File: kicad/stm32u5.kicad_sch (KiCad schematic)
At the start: 10 parts, among them SW5 BOOTSEL, U12 STM32U535CET6-modified

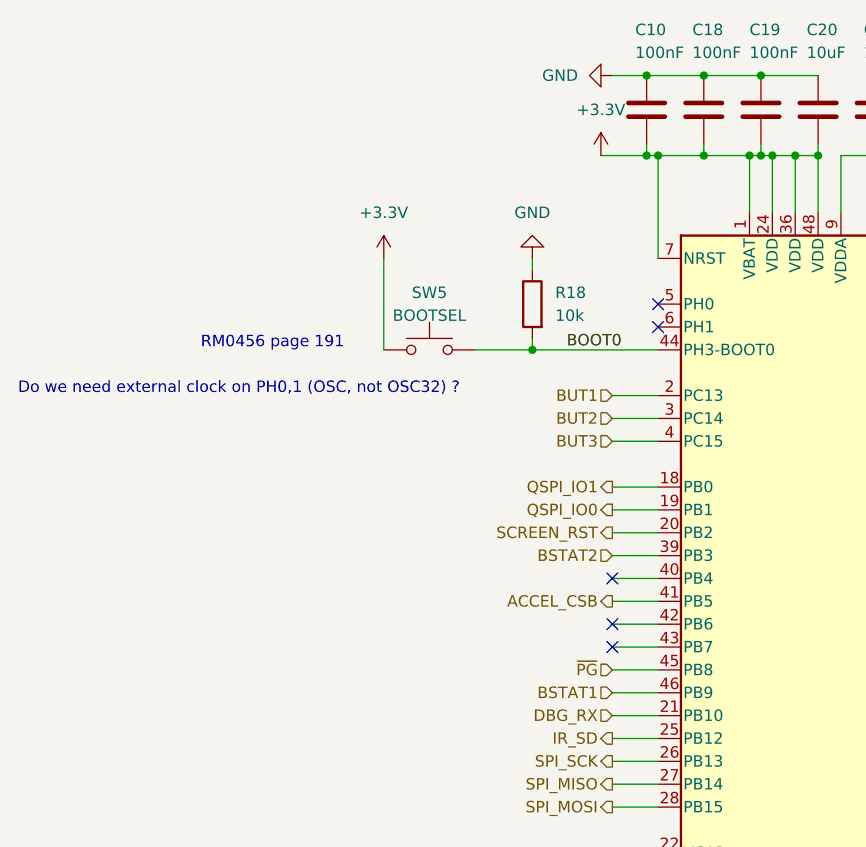
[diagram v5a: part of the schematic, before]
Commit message: hw: change battery to a "simpler" version
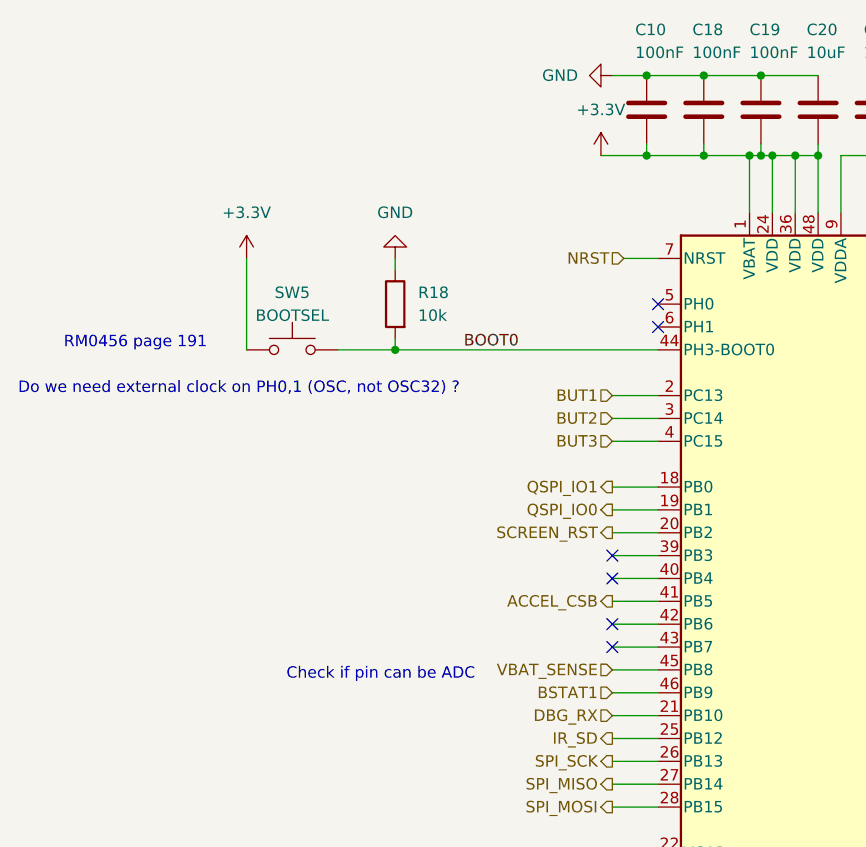
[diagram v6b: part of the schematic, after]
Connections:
- net +3.3V: no longer U12.7 (NRST)
- net BSTAT2: no longer names the net of U12.39 (PB3)
- net ~{PG} renamed VBAT_SENSE
- new net NRST: U12.7 (NRST)
- no-connect marks 5 -> 6
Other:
- note added: "Check if pin can be ADC"
- moved on the sheet: R18, SW5
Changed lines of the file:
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@@
   (junction (at 105.41 33.02) (diameter 0) (color 0 0 0 0)
   )
-  (junction (at 86.36 54.61) (diameter 0) (color 0 0 0 0)
+  (junction (at 71.12 54.61) (diameter 0) (color 0 0 0 0)
   )
   (junction (at 130.81 24.13) (diameter 0) (color 0 0 0 0)
-  )
-  (junction (at 100.33 33.02) (diameter 0) (color 0 0 0 0)
   )
   (junction (at 96.52 119.38) (diameter 0) (color 0 0 0 0)
@@
   (no_connect (at 95.25 87.63))
   (no_connect (at 100.33 49.53))
+  (no_connect (at 95.25 77.47))
   (wire (pts (xy 115.57 33.02) (xy 118.11 33.02))
     (stroke (width 0) (type default))
@@
     (stroke (width 0) (type default))
   )
+  (wire (pts (xy 96.52 44.45) (xy 100.33 44.45))
+    (stroke (width 0) (type default))
+  )
   (wire (pts (xy 130.81 24.13) (xy 137.16 24.13))
     (stroke (width 0) (type default))
@@
     (stroke (width 0) (type default))
   )
-  (wire (pts (xy 99.06 33.02) (xy 100.33 33.02))
+  (wire (pts (xy 99.06 33.02) (xy 105.41 33.02))
     (stroke (width 0) (type default))
   )
@@
     (stroke (width 0) (type default))
   )
+  (wire (pts (xy 71.12 54.61) (xy 100.33 54.61))
+    (stroke (width 0) (type default))
+  )
   (wire (pts (xy 95.25 92.71) (xy 100.33 92.71))
     (stroke (width 0) (type default))
@@
     (stroke (width 0) (type default))
   )
-  (wire (pts (xy 100.33 33.02) (xy 100.33 44.45))
-    (stroke (width 0) (type default))
-  )
   (wire (pts (xy 118.11 119.38) (xy 118.11 118.11))
     (stroke (width 0) (type default))
@@
     (stroke (width 0) (type default))
   )
-  (wire (pts (xy 69.85 44.45) (xy 69.85 54.61))
+  (wire (pts (xy 54.61 44.45) (xy 54.61 54.61))
     (stroke (width 0) (type default))
   )
@@
     (stroke (width 0) (type default))
   )
-  (wire (pts (xy 86.36 54.61) (xy 100.33 54.61))
-    (stroke (width 0) (type default))
-  )
   (wire (pts (xy 118.11 33.02) (xy 118.11 39.37))
     (stroke (width 0) (type default))
   )
-  (wire (pts (xy 86.36 53.34) (xy 86.36 54.61))
+  (wire (pts (xy 71.12 53.34) (xy 71.12 54.61))
     (stroke (width 0) (type default))
   )
@@
     (stroke (width 0) (type default))
   )
-  (wire (pts (xy 86.36 44.45) (xy 86.36 45.72))
+  (wire (pts (xy 71.12 44.45) (xy 71.12 45.72))
     (stroke (width 0) (type default))
   )
@@
     (stroke (width 0) (type default))
   )
-  (wire (pts (xy 80.01 54.61) (xy 86.36 54.61))
+  (wire (pts (xy 64.77 54.61) (xy 71.12 54.61))
     (stroke (width 0) (type default))
   )
@@
   )
   (wire (pts (xy 113.03 33.02) (xy 115.57 33.02))
-    (stroke (width 0) (type default))
-  )
-  (wire (pts (xy 100.33 33.02) (xy 105.41 33.02))
     (stroke (width 0) (type default))
   )
@@
     (effects (font (size 1.27 1.27)) (justify left bottom))
   )
-  (text "RM0456 page 191" (at 49.53 54.61 0)
+  (text "RM0456 page 191" (at 34.29 54.61 0)
     (effects (font (size 1.27 1.27)) (justify left bottom))
   )
@@
     (effects (font (size 1.27 1.27)) (justify left bottom))
   )
+  (text "Check if pin can be ADC" (at 80.01 91.44 0)
+    (effects (font (size 1.27 1.27)) (justify right bottom))
+  )
   (text "Comparator needs analogue function" (at 163.83 82.55 0)
     (effects (font (size 1.27 1.27)) (justify left bottom))
@@
     (effects (font (size 1.27 1.27)) (justify left bottom))
   )
-  (label "BOOT0" (at 90.17 54.61 0) (fields_autoplaced)
+  (label "BOOT0" (at 78.74 54.61 0) (fields_autoplaced)
     (effects (font (size 1.27 1.27)) (justify left bottom))
   )
@@
     (effects (font (size 1.27 1.27)) (justify right))
   )
+  (hierarchical_label "NRST" (shape input) (at 96.52 44.45 180) (fields_autoplaced)
+    (effects (font (size 1.27 1.27)) (justify right))
+  )
   (hierarchical_label "EEPROM_CSB" (shape output) (at 135.89 64.77 0) (fields_autoplaced)
     (effects (font (size 1.27 1.27)) (justify left))
@@
     (effects (font (size 1.27 1.27)) (justify right))
   )
-  (hierarchical_label "~{PG}" (shape input) (at 95.25 90.17 180) (fields_autoplaced)
-    (effects (font (size 1.27 1.27)) (justify right))
-  )
   (hierarchical_label "WKUP1" (shape input) (at 135.89 44.45 0) (fields_autoplaced)
     (effects (font (size 1.27 1.27)) (justify left))
@@
     (effects (font (size 1.27 1.27)) (justify right))
   )
+  (hierarchical_label "VBAT_SENSE" (shape input) (at 95.25 90.17 180) (fields_autoplaced)
+    (effects (font (size 1.27 1.27)) (justify right))
+  )
   (hierarchical_label "QSPI_IO3" (shape output) (at 135.89 59.69 0) (fields_autoplaced)
     (effects (font (size 1.27 1.27)) (justify left))
@@
   (hierarchical_label "USB_DP" (shape input) (at 135.89 74.93 0) (fields_autoplaced)
     (effects (font (size 1.27 1.27)) (justify left))
-  )
-  (hierarchical_label "BSTAT2" (shape input) (at 95.25 77.47 180) (fields_autoplaced)
-    (effects (font (size 1.27 1.27)) (justify right))
   )
   (hierarchical_label "DBG_RX" (shape input) (at 95.25 95.25 180) (fields_autoplaced)
@@
     )
   )
-  (symbol (lib_id "Device:R") (at 86.36 49.53 0) (mirror y) (unit 1)
-    (in_bom yes) (on_board yes) (dnp no) (fields_autoplaced)
-    (property "Reference" "R18" (at 88.9 48.26 0)
+  (symbol (lib_id "Device:R") (at 71.12 49.53 0) (mirror y) (unit 1)
+    (in_bom yes) (on_board yes) (dnp no) (fields_autoplaced)
+    (property "Reference" "R18" (at 73.66 48.26 0)
       (effects (font (size 1.27 1.27)) (justify right))
     )
-    (property "Value" "10k" (at 88.9 50.8 0)
+    (property "Value" "10k" (at 73.66 50.8 0)
       (effects (font (size 1.27 1.27)) (justify right))
     )
-    (property "Footprint" "Capacitor_SMD:C_0402_1005Metric" (at 88.138 49.53 90)
-      (effects (font (size 1.27 1.27)) hide)
-    )
-    (property "Datasheet" "~" (at 86.36 49.53 0)
+    (property "Footprint" "Capacitor_SMD:C_0402_1005Metric" (at 72.898 49.53 90)
+      (effects (font (size 1.27 1.27)) hide)
+    )
+    (property "Datasheet" "~" (at 71.12 49.53 0)
       (effects (font (size 1.27 1.27)) hide)
     )
@@
     )
   )
-  (symbol (lib_id "power:GND") (at 86.36 44.45 180) (unit 1)
-    (in_bom yes) (on_board yes) (dnp no) (fields_autoplaced)
-    (property "Reference" "#PWR08" (at 86.36 38.1 0)
-      (effects (font (size 1.27 1.27)) hide)
-    )
-    (property "Value" "GND" (at 86.36 39.37 0)
+  (symbol (lib_id "power:GND") (at 71.12 44.45 180) (unit 1)
+    (in_bom yes) (on_board yes) (dnp no) (fields_autoplaced)
+    (property "Reference" "#PWR08" (at 71.12 38.1 0)
+      (effects (font (size 1.27 1.27)) hide)
+    )
+    (property "Value" "GND" (at 71.12 39.37 0)
       (effects (font (size 1.27 1.27)))
     )
-    (property "Footprint" "" (at 86.36 44.45 0)
-      (effects (font (size 1.27 1.27)) hide)
-    )
-    (property "Datasheet" "" (at 86.36 44.45 0)
+    (property "Footprint" "" (at 71.12 44.45 0)
+      (effects (font (size 1.27 1.27)) hide)
+    )
+    (property "Datasheet" "" (at 71.12 44.45 0)
       (effects (font (size 1.27 1.27)) hide)
     )
@@
     )
   )
-  (symbol (lib_id "power:+3.3V") (at 69.85 44.45 0) (unit 1)
-    (in_bom yes) (on_board yes) (dnp no) (fields_autoplaced)
-    (property "Reference" "#PWR07" (at 69.85 48.26 0)
-      (effects (font (size 1.27 1.27)) hide)
-    )
-    (property "Value" "+3.3V" (at 69.85 39.37 0)
+  (symbol (lib_id "power:+3.3V") (at 54.61 44.45 0) (unit 1)
+    (in_bom yes) (on_board yes) (dnp no) (fields_autoplaced)
+    (property "Reference" "#PWR07" (at 54.61 48.26 0)
+      (effects (font (size 1.27 1.27)) hide)
+    )
+    (property "Value" "+3.3V" (at 54.61 39.37 0)
       (effects (font (size 1.27 1.27)))
     )
-    (property "Footprint" "" (at 69.85 44.45 0)
-      (effects (font (size 1.27 1.27)) hide)
-    )
-    (property "Datasheet" "" (at 69.85 44.45 0)
+    (property "Footprint" "" (at 54.61 44.45 0)
+      (effects (font (size 1.27 1.27)) hide)
+    )
+    (property "Datasheet" "" (at 54.61 44.45 0)
       (effects (font (size 1.27 1.27)) hide)
     )
@@
     )
   )
-  (symbol (lib_id "Switch:SW_Push") (at 74.93 54.61 0) (unit 1)
-    (in_bom yes) (on_board yes) (dnp no) (fields_autoplaced)
-    (property "Reference" "SW5" (at 74.93 48.26 0)
+  (symbol (lib_id "Switch:SW_Push") (at 59.69 54.61 0) (unit 1)
+    (in_bom yes) (on_board yes) (dnp no) (fields_autoplaced)
+    (property "Reference" "SW5" (at 59.69 48.26 0)
       (effects (font (size 1.27 1.27)))
     )
-    (property "Value" "BOOTSEL" (at 74.93 50.8 0)
+    (property "Value" "BOOTSEL" (at 59.69 50.8 0)
       (effects (font (size 1.27 1.27)))
     )
-    (property "Footprint" "Jumper:SolderJumper-2_P1.3mm_Open_Pad1.0x1.5mm" (at 74.93 49.53 0)
-      (effects (font (size 1.27 1.27)) hide)
-    )
-    (property "Datasheet" "~" (at 74.93 49.53 0)
-      (effects (font (size 1.27 1.27)) hide)
-    )
+    (property "Footprint" "Jumper:SolderJumper-2_P1.3mm_Open_Pad1.0x1.5mm" (at 59.69 49.53 0)
+      (effects (font (size 1.27 1.27)) hide)
+    )
+    (property "Datasheet" "~" (at 59.69 49.53 0)
+      (effects (font (size 1.27 1.27)) hide)
+    )
